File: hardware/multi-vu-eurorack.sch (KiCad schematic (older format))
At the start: 63 parts

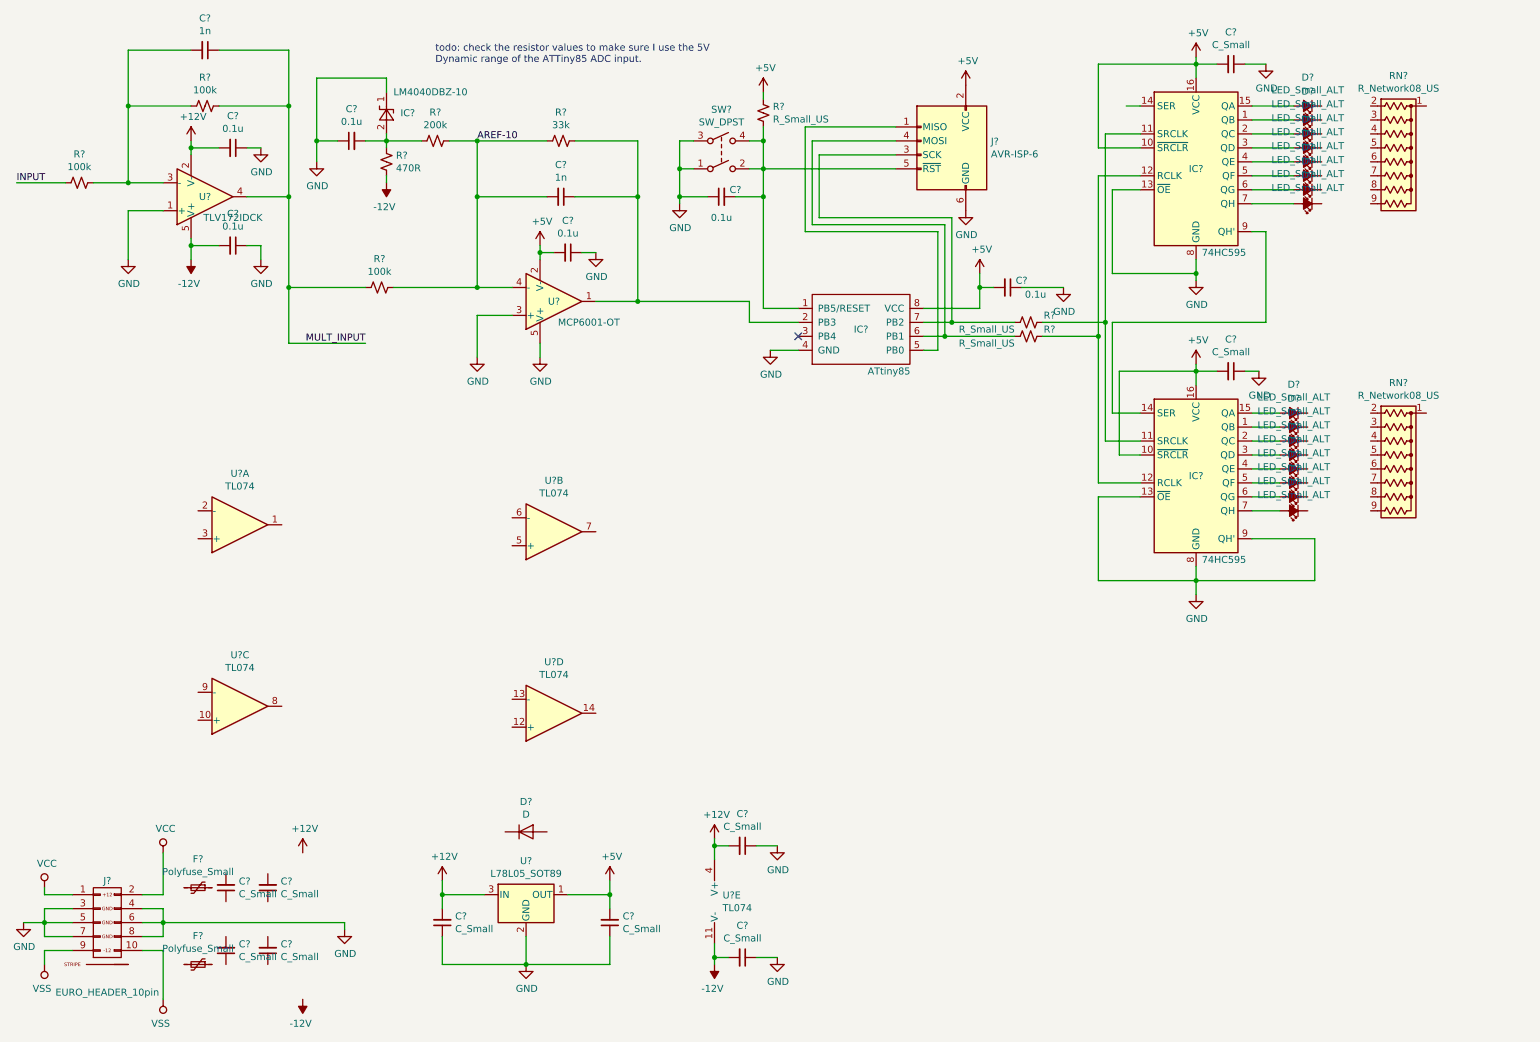
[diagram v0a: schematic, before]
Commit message: Added values and annotations to the schematic. Added feedback loops and resistors to TL074 Mult Output amps. Added some notes to self.
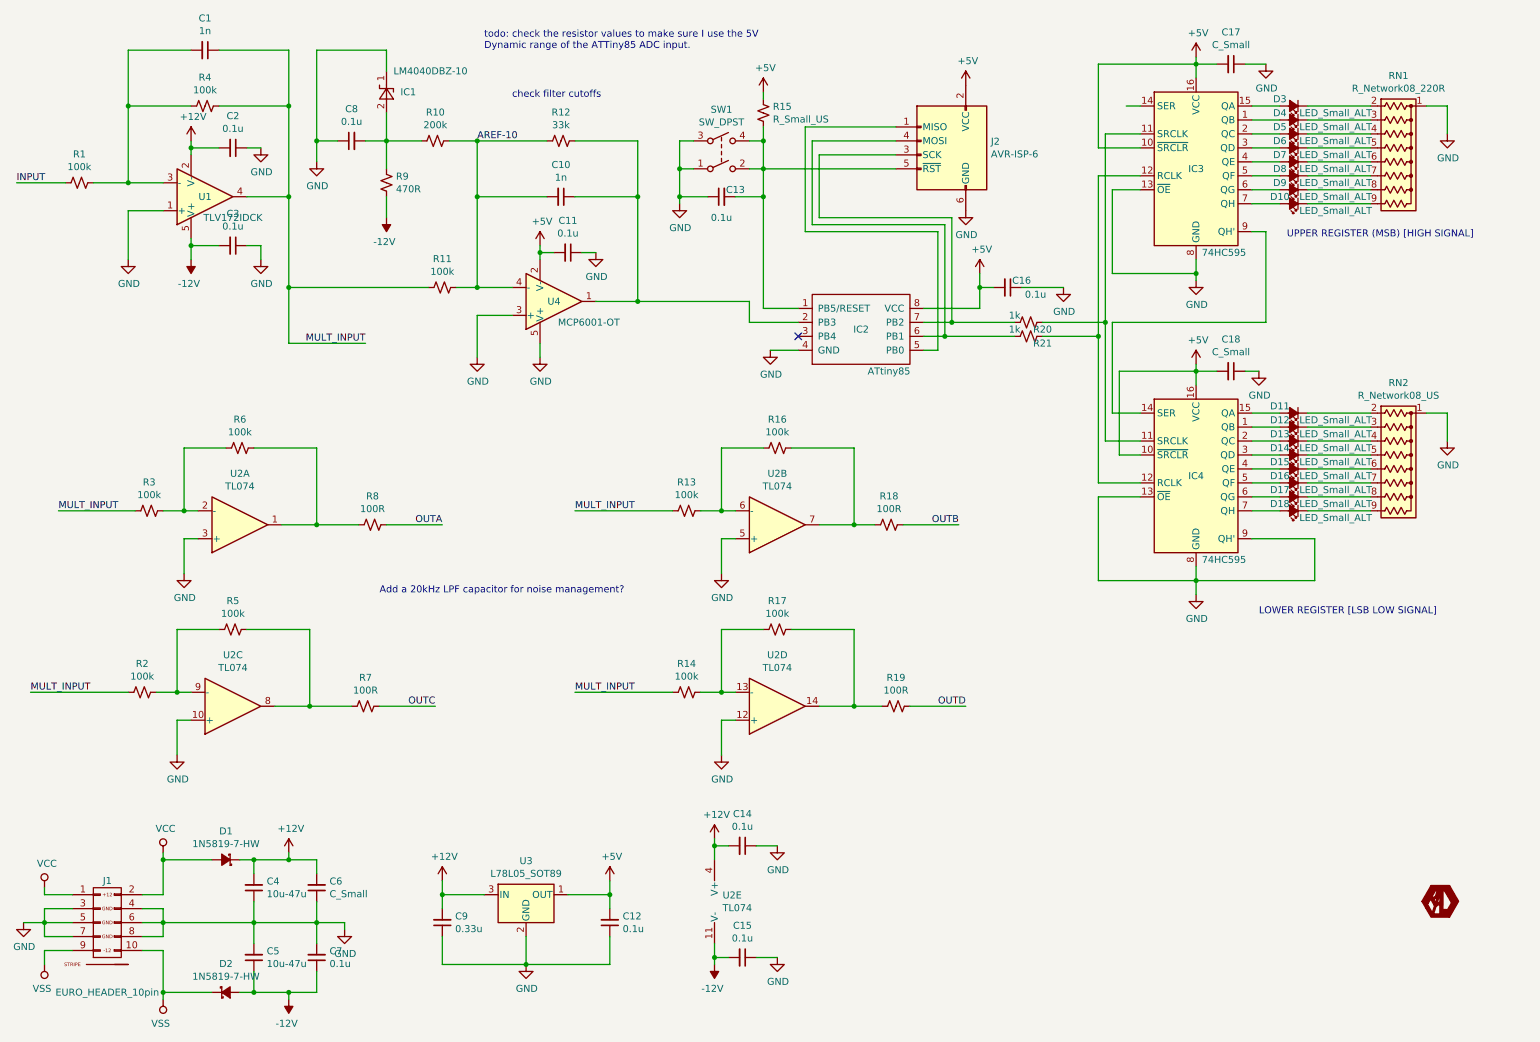
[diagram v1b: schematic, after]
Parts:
- removed D? (x8): LED_Small_ALT, symbol Device:LED_Small_ALT
- removed D?: D, symbol Device:D
- removed F? (x2): Polyfuse_Small, symbol Device:Polyfuse_Small
- removed RN?: R_Network08_US, Resistor_THT:R_Array_SIP9, symbol Device:R_Network08_US
- added D1, D2: 1N5819-7-HW, symbol Device:D_Schottky_Small_ALT
- added D10, D3, D4, D5, D6, D7, D8, D9: LED_Small_ALT, symbol Device:LED_Small_ALT
- added R13, R14, R16, R17, R2, R3, R5, R6: 100k, symbol Device:R_Small_US
- added R18, R19, R7, R8: 100R, symbol Device:R_Small_US
- added RN1: R_Network08_220R, Resistor_SMD:R_Cat16-8, symbol Device:R_Network08_US
- C12, C14, C15, C7: renamed from C?; value C_Small -> 0.1u
- C4, C5: renamed from C?; value C_Small -> 10u-47u
- C9: renamed from C?; value C_Small -> 0.33u
- R20, R21: renamed from R?; value R_Small_US -> 1k
- gave numbers to parts that had none: 38
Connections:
- net +12V: now also C4.2, C6.2, D1.1 (K)
- net -12V: now also C5.1, C7.1, D2.2 (A)
- net GND: now also C4.1, C5.2, C6.1, C7.2, RN2.1 (common), U2.10 (+), U2.12 (+), U2.3 (+), U2.5 (+), RN1.1 (common)
- net MULT_INPUT: now also R13.2, R14.2, R2.2, R3.2
- net VCC: now also D1.2 (A)
- net VSS: now also D2.1 (K)
- net at IC3.1 (QB): now also D4.2 (A)
- net at IC3.15 (QA): now also D3.2 (A)
- net at IC3.2 (QC): now also D5.2 (A)
- net at IC3.3 (QD): now also D6.2 (A)
- net at IC3.4 (QE): now also D7.2 (A)
- net at IC3.5 (QF): now also D8.2 (A)
- net at IC3.6 (QG): now also D9.2 (A)
- net at IC3.7 (QH): now also D10.2 (A)
- net at U2.1: now also R6.1, R8.2
- net at U2.2 (-): now also R3.1, R6.2
- net at U2.6 (-): now also R13.1, R16.2
- net at U2.7: now also R16.1, R18.2
- net at U2.8: now also R5.1, R7.2
- net at U2.9 (-): now also R2.1, R5.2
- net at U2.13 (-): now also R14.1, R17.2
- net at U2.14: now also R17.1, R19.2
- net at D11.1 (K): now also RN2.2 (R1)
- net at D12.1 (K): now also RN2.3 (R2)
- net at D13.1 (K): now also RN2.4 (R3)
- net at D14.1 (K): now also RN2.5 (R4)
- net at D15.1 (K): now also RN2.6 (R5)
- net at D16.1 (K): now also RN2.7 (R6)
- net at D17.1 (K): now also RN2.8 (R7)
- net at D18.1 (K): now also RN2.9 (R8)
- new net: D4.1 (K), RN1.3 (R2)
- new net: D5.1 (K), RN1.4 (R3)
- new net: D6.1 (K), RN1.5 (R4)
- new net: D7.1 (K), RN1.6 (R5)
- new net: D8.1 (K), RN1.7 (R6)
- new net: D9.1 (K), RN1.8 (R7)
- new net: D10.1 (K), RN1.9 (R8)
- new net: D3.1 (K), RN1.2 (R1)
- new net OUTA: R8.1
- new net OUTB: R18.1
- new net OUTC: R7.1
- new net OUTD: R19.1
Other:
- note added: "Add a 20kHz LPF capacitor for noise management?"
- note added: "LOWER REGISTER [LSB LOW SIGNAL]"
- note added: "UPPER REGISTER (MSB) [HIGH SIGNAL]"
- note added: "check filter cutoffs"
- moved on the sheet: C4, C5, C6, C7, IC1, R11, R9, U2B, U2C, U2D

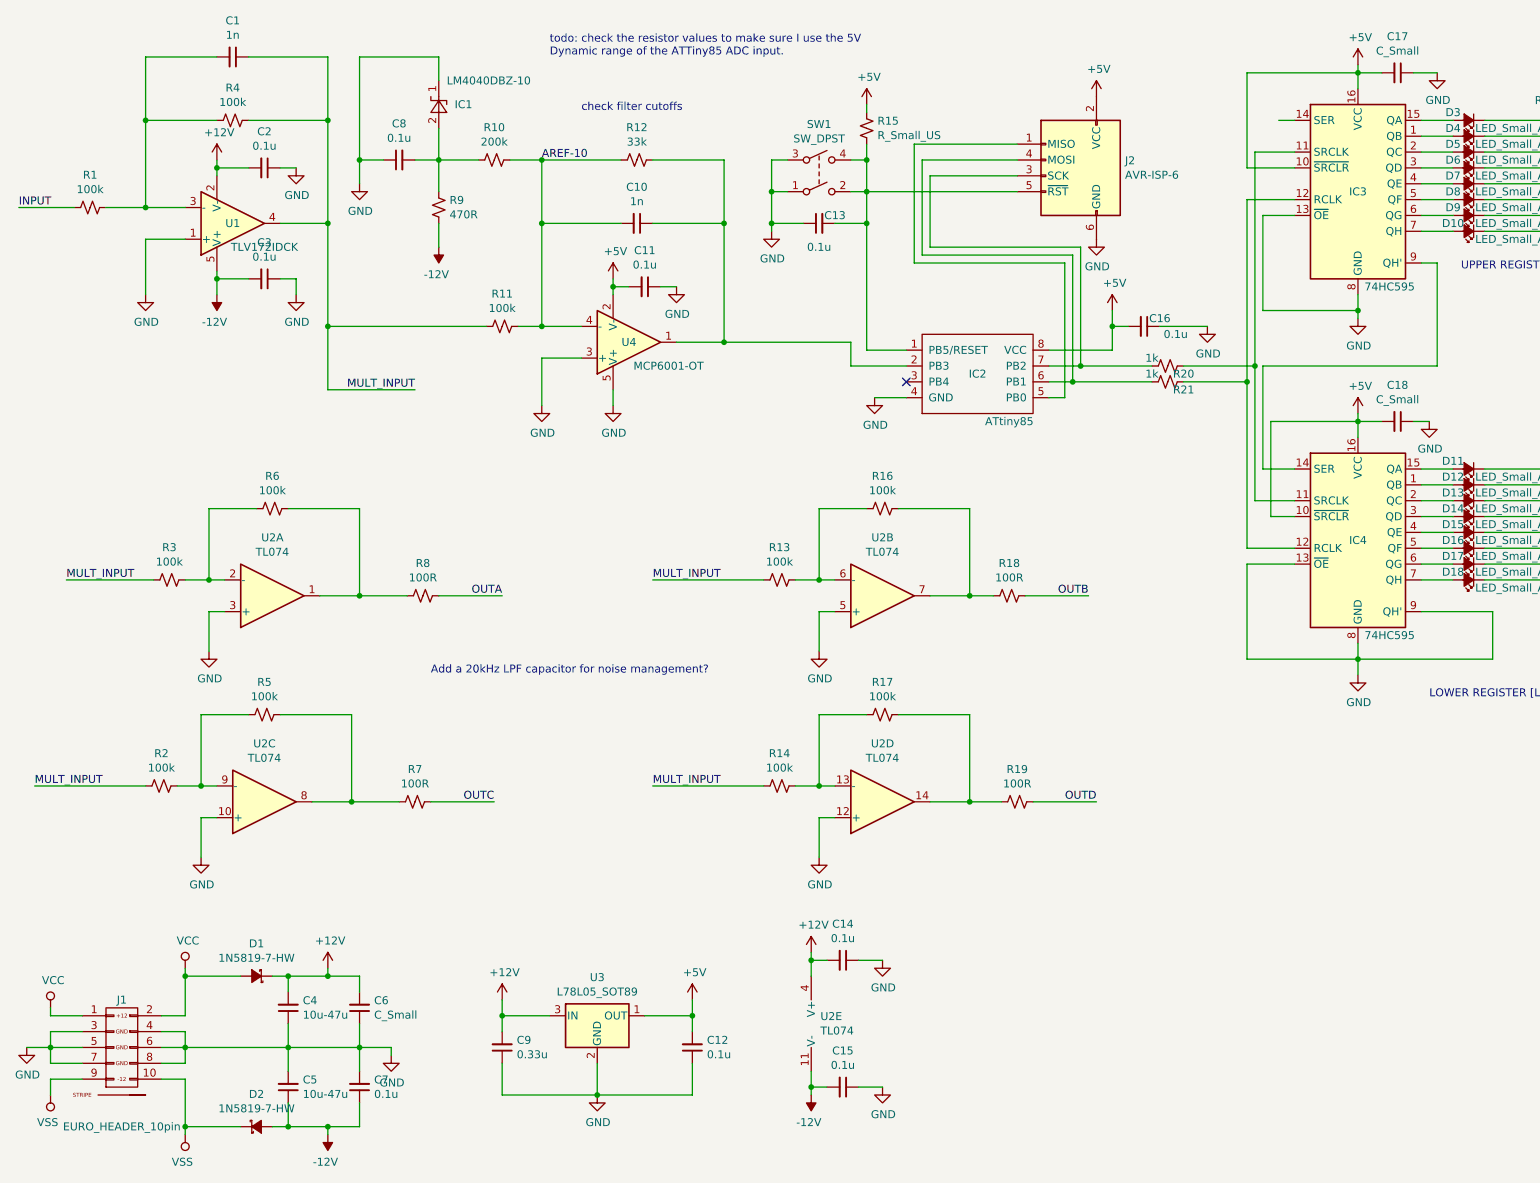
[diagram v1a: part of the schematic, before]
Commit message: Added footprints to components in schematic. Started PCB layout and grouping subcircuits together in PCBNew.
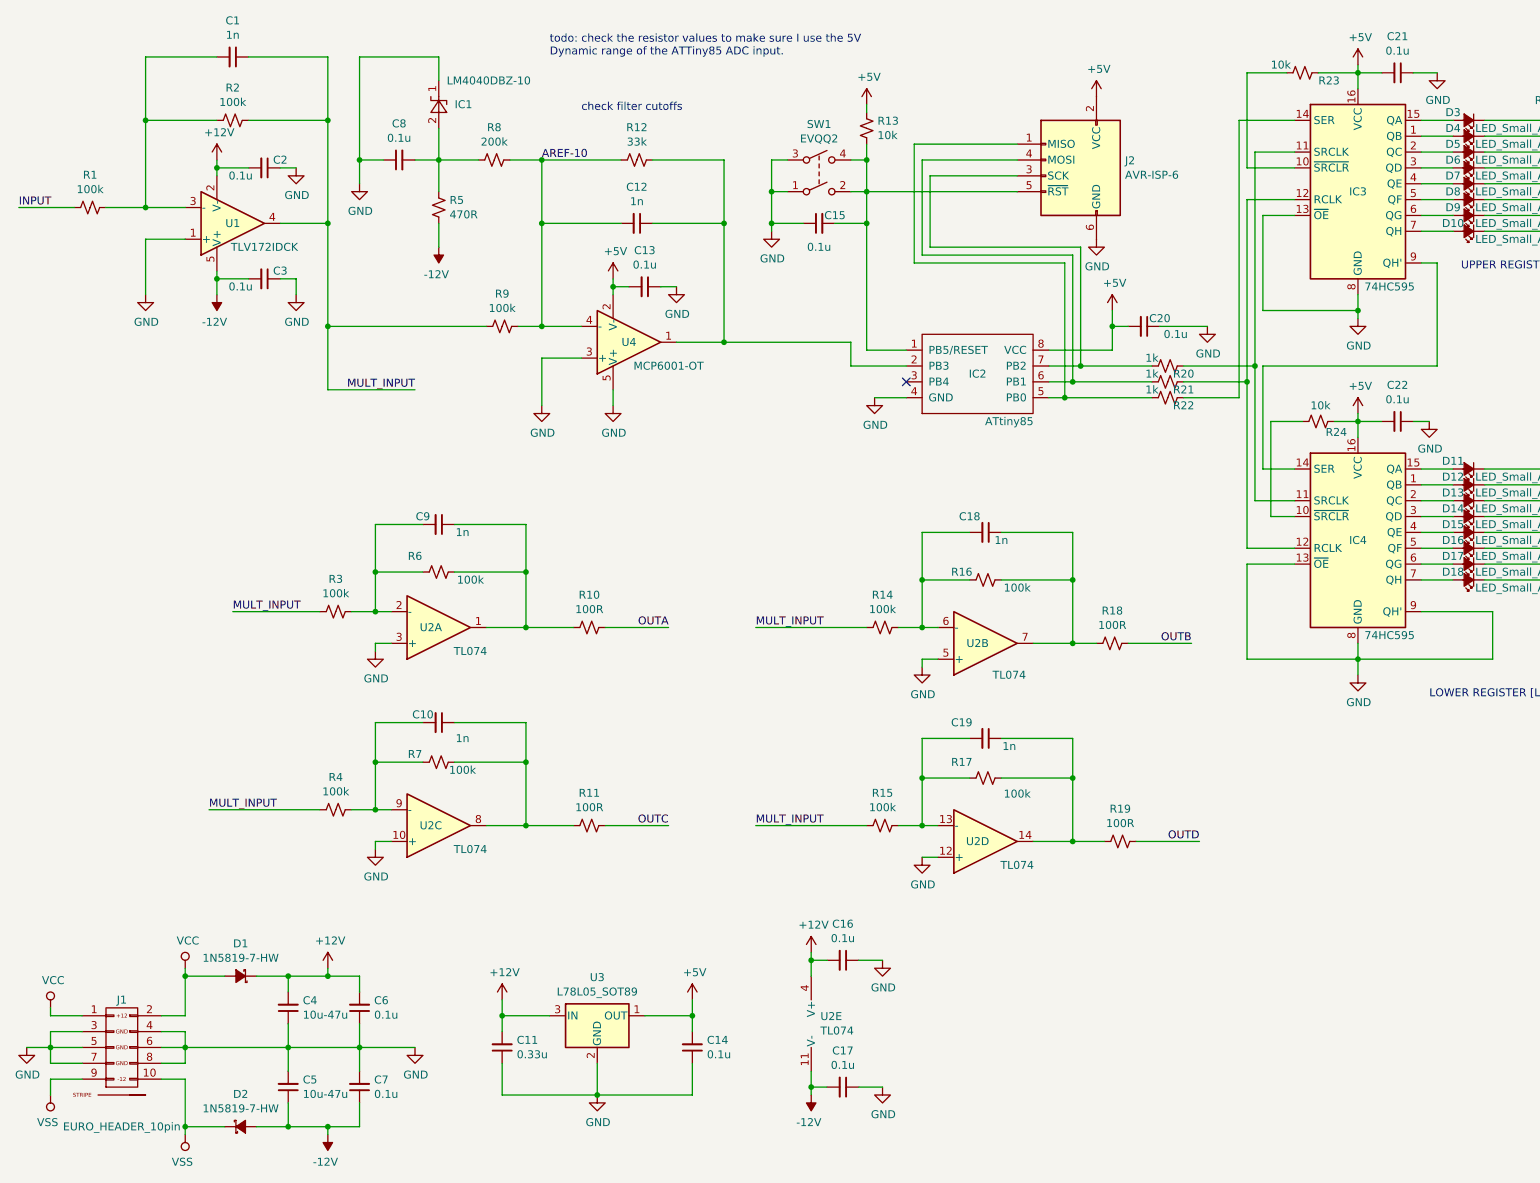
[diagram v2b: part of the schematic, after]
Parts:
- added C10, C18, C19, C9: 1n, Capacitor_SMD:C_0603_1608Metric_Pad1.05x0.95mm_HandSolder, symbol 4ms-passives:C_Small
- added R22: 1k, Capacitor_SMD:C_0603_1608Metric_Pad1.05x0.95mm_HandSolder, symbol Device:R_Small_US
- added R23, R24: 10k, Capacitor_SMD:C_0603_1608Metric_Pad1.05x0.95mm_HandSolder, symbol Device:R_Small_US
- C1, C2, C3, C4, C5, C7, C8, R1, R12, R16, R17, R18, R19, R20, R21, R3, R6: footprint (none) -> Capacitor_SMD:C_0603_1608Metric_Pad1.05x0.95mm_HandSolder
- C11: renamed from C9; footprint (none) -> Capacitor_SMD:C_0603_1608Metric_Pad1.05x0.95mm_HandSolder
- C12: renamed from C10; footprint (none) -> Capacitor_SMD:C_0603_1608Metric_Pad1.05x0.95mm_HandSolder
- C13: renamed from C11; footprint (none) -> Capacitor_SMD:C_0603_1608Metric_Pad1.05x0.95mm_HandSolder
- C14: renamed from C12; footprint (none) -> Capacitor_SMD:C_0603_1608Metric_Pad1.05x0.95mm_HandSolder
- C15: renamed from C13; footprint (none) -> Capacitor_SMD:C_0603_1608Metric_Pad1.05x0.95mm_HandSolder
- C16: renamed from C14; footprint (none) -> Capacitor_SMD:C_0603_1608Metric_Pad1.05x0.95mm_HandSolder
- C17: renamed from C15; footprint (none) -> Capacitor_SMD:C_0603_1608Metric_Pad1.05x0.95mm_HandSolder
- C20: renamed from C16; footprint (none) -> Capacitor_SMD:C_0603_1608Metric_Pad1.05x0.95mm_HandSolder
- C21: renamed from C17; value C_Small -> 0.1u; footprint (none) -> Capacitor_SMD:C_0603_1608Metric_Pad1.05x0.95mm_HandSolder
- C22: renamed from C18; value C_Small -> 0.1u; footprint (none) -> Capacitor_SMD:C_0603_1608Metric_Pad1.05x0.95mm_HandSolder
- C6: value C_Small -> 0.1u; footprint (none) -> Capacitor_SMD:C_0603_1608Metric_Pad1.05x0.95mm_HandSolder
- D1, D2: footprint (none) -> Diode_SMD:D_SOD-323_HandSoldering
- D10, D11, D12, D13, D14, D15, D16, D17, D18, D3, D4, D5, D6, D7, D8, D9: footprint (none) -> LED_SMD:LED_0603_1608Metric_Pad1.05x0.95mm_HandSolder
- IC2: footprint (none) -> Package_SO:SOIC-8_3.9x4.9mm_P1.27mm
- IC3, IC4, U2: footprint (none) -> Package_SO:TSSOP-14_4.4x5mm_P0.65mm
- J2: footprint (none) -> Connector_PinHeader_2.54mm:PinHeader_2x03_P2.54mm_Vertical
- R10: renamed from R8; footprint (none) -> Capacitor_SMD:C_0603_1608Metric_Pad1.05x0.95mm_HandSolder
- R11: renamed from R7; footprint (none) -> Capacitor_SMD:C_0603_1608Metric_Pad1.05x0.95mm_HandSolder
- R13: renamed from R15; value R_Small_US -> 10k; footprint (none) -> Capacitor_SMD:C_0603_1608Metric_Pad1.05x0.95mm_HandSolder
- R14: renamed from R13; footprint (none) -> Capacitor_SMD:C_0603_1608Metric_Pad1.05x0.95mm_HandSolder
- R15: renamed from R14; footprint (none) -> Capacitor_SMD:C_0603_1608Metric_Pad1.05x0.95mm_HandSolder
- R2: renamed from R4; footprint (none) -> Capacitor_SMD:C_0603_1608Metric_Pad1.05x0.95mm_HandSolder
- R4: renamed from R2; footprint (none) -> Capacitor_SMD:C_0603_1608Metric_Pad1.05x0.95mm_HandSolder
- R5: renamed from R9; footprint (none) -> Capacitor_SMD:C_0603_1608Metric_Pad1.05x0.95mm_HandSolder
- R7: renamed from R5; footprint (none) -> Capacitor_SMD:C_0603_1608Metric_Pad1.05x0.95mm_HandSolder
- R8: renamed from R10; footprint (none) -> Capacitor_SMD:C_0603_1608Metric_Pad1.05x0.95mm_HandSolder
- R9: renamed from R11; footprint (none) -> Capacitor_SMD:C_0603_1608Metric_Pad1.05x0.95mm_HandSolder
- RN1: footprint Resistor_SMD:R_Cat16-8 -> CAY17-331JALF:RESCAXS64P320X160X60-10N
- RN2: footprint Resistor_THT:R_Array_SIP9 -> CAY17-331JALF:RESCAXS64P320X160X60-10N
- SW1: value SW_DPST -> EVQQ2; footprint (none) -> Button_Switch_SMD:SW_SPST_EVQQ2
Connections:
- net +5V: now also R23.1, R24.1; no longer IC3.10 (~SRCLR), IC4.10 (~SRCLR)
- net at IC2.5 (PB0), J2.1 (MISO): now also R22.2
- net at IC3.14 (SER): now also R22.1
- net at R3.1, R6.2, U2.2 (-): now also C9.2
- net at R10.2, R6.1, U2.1: now also C9.1
- net at R14.1, R16.2, U2.6 (-): now also C18.2
- net at R16.1, R18.2, U2.7: now also C18.1
- net at R11.2, R7.1, U2.8: now also C10.1
- net at R4.1, R7.2, U2.9 (-): now also C10.2
- net at R15.1, R17.2, U2.13 (-): now also C19.2
- net at R17.1, R19.2, U2.14: now also C19.1
- new net: IC3.10 (~SRCLR), R23.2
- new net: IC4.10 (~SRCLR), R24.2
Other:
- note removed: "Add a 20kHz LPF capacitor for noise management?"
- moved on the sheet: D1, D2, R10, R11, R14, R15, R16, R17, R18, R19, R3, R4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
